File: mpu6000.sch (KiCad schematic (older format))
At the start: 9 parts

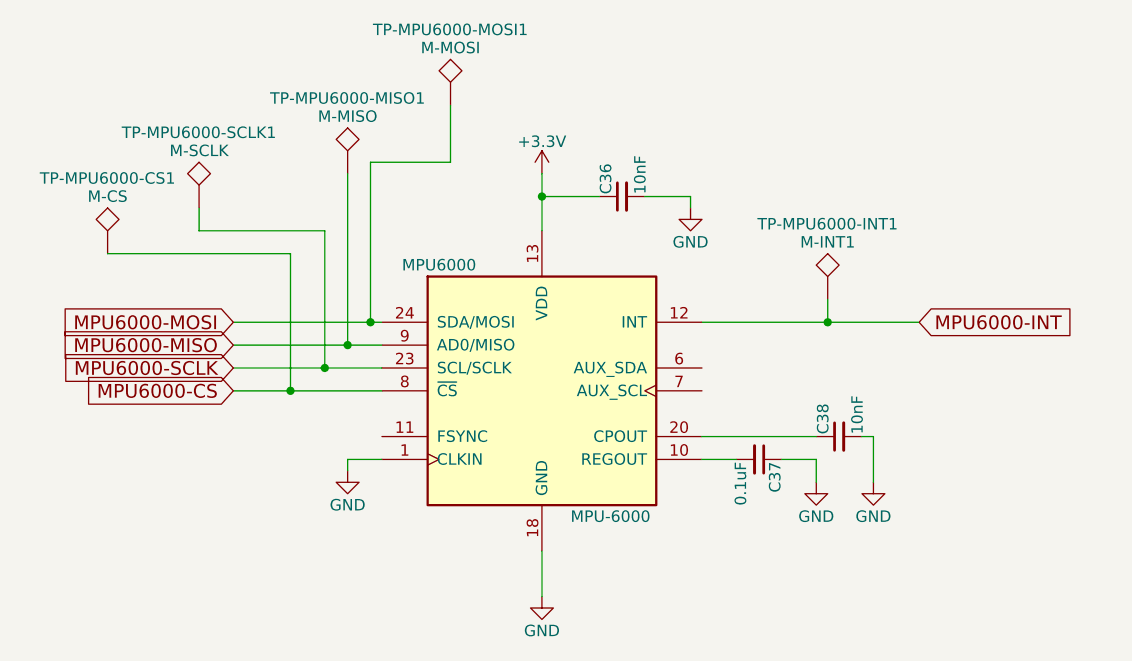
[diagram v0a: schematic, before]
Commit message: tp name fixes
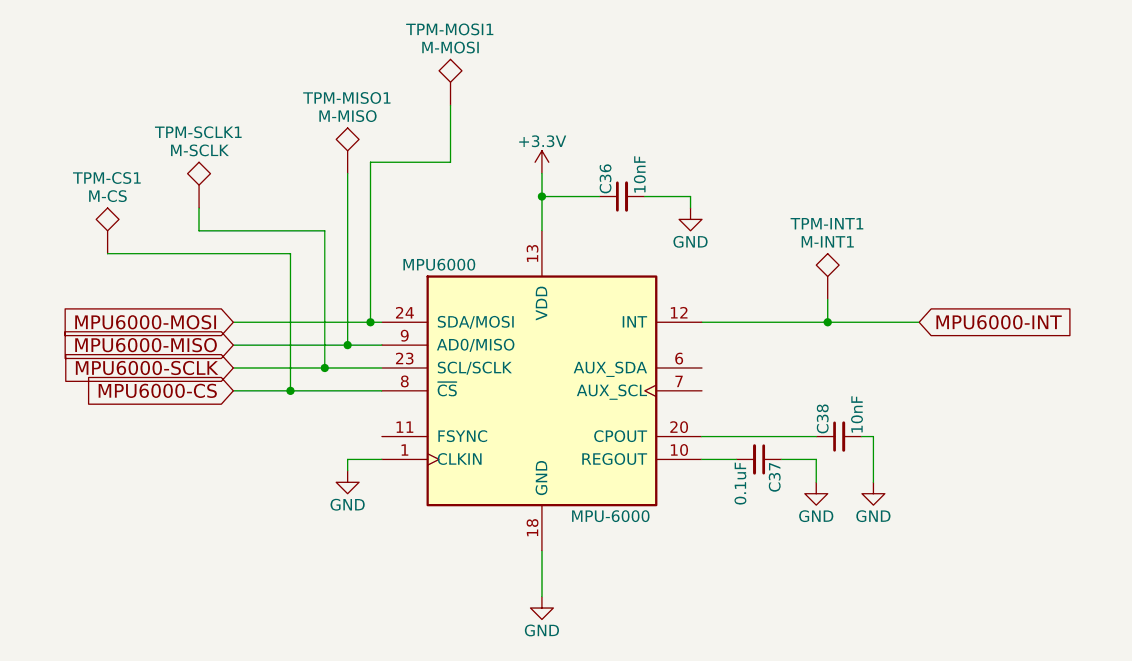
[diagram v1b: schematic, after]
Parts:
- renumbered TP-MPU6000-CS1 to TPM-CS1, TP-MPU6000-INT1 to TPM-INT1, TP-MPU6000-MISO1 to TPM-MISO1, TP-MPU6000-MOSI1 to TPM-MOSI1, TP-MPU6000-SCLK1 to TPM-SCLK1
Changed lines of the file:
@@
 	5100 4100 5100 4150
 $Comp
-L TEST TP-MPU6000-CS1
+L TEST TPM-CS1
 U 1 1 5B3F20EC
 P 4050 3200
-F 0 "TP-MPU6000-CS1" H 4050 3500 50  0000 C BNN
+F 0 "TPM-CS1" H 4050 3500 50  0000 C BNN
 F 1 "M-CS" H 4050 3450 50  0000 C CNN
 F 2 "Measurement_Points:Measurement_Point_Round-SMD-Pad_Small" H 4050 3200 50  0001 C CNN
@@
 $EndComp
 $Comp
-L TEST TP-MPU6000-SCLK1
+L TEST TPM-SCLK1
 U 1 1 5B3F20FE
 P 4450 3000
-F 0 "TP-MPU6000-SCLK1" H 4450 3300 50  0000 C BNN
+F 0 "TPM-SCLK1" H 4450 3300 50  0000 C BNN
 F 1 "M-SCLK" H 4450 3250 50  0000 C CNN
 F 2 "Measurement_Points:Measurement_Point_Round-SMD-Pad_Small" H 4450 3000 50  0001 C CNN
@@
 $EndComp
 $Comp
-L TEST TP-MPU6000-MISO1
+L TEST TPM-MISO1
 U 1 1 5B3F2136
 P 5100 2850
-F 0 "TP-MPU6000-MISO1" H 5100 3150 50  0000 C BNN
+F 0 "TPM-MISO1" H 5100 3150 50  0000 C BNN
 F 1 "M-MISO" H 5100 3100 50  0000 C CNN
 F 2 "Measurement_Points:Measurement_Point_Round-SMD-Pad_Small" H 5100 2850 50  0001 C CNN
@@
 $EndComp
 $Comp
-L TEST TP-MPU6000-MOSI1
+L TEST TPM-MOSI1
 U 1 1 5B3F216D
 P 5550 2550
-F 0 "TP-MPU6000-MOSI1" H 5550 2850 50  0000 C BNN
+F 0 "TPM-MOSI1" H 5550 2850 50  0000 C BNN
 F 1 "M-MOSI" H 5550 2800 50  0000 C CNN
 F 2 "Measurement_Points:Measurement_Point_Round-SMD-Pad_Small" H 5550 2550 50  0001 C CNN
@@
 $EndComp
 $Comp
-L TEST TP-MPU6000-INT1
+L TEST TPM-INT1
 U 1 1 5B3F2199
 P 7200 3400
-F 0 "TP-MPU6000-INT1" H 7200 3700 50  0000 C BNN
+F 0 "TPM-INT1" H 7200 3700 50  0000 C BNN
 F 1 "M-INT1" H 7200 3650 50  0000 C CNN
 F 2 "Measurement_Points:Measurement_Point_Round-SMD-Pad_Small" H 7200 3400 50  0001 C CNN

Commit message: Name changes on silk
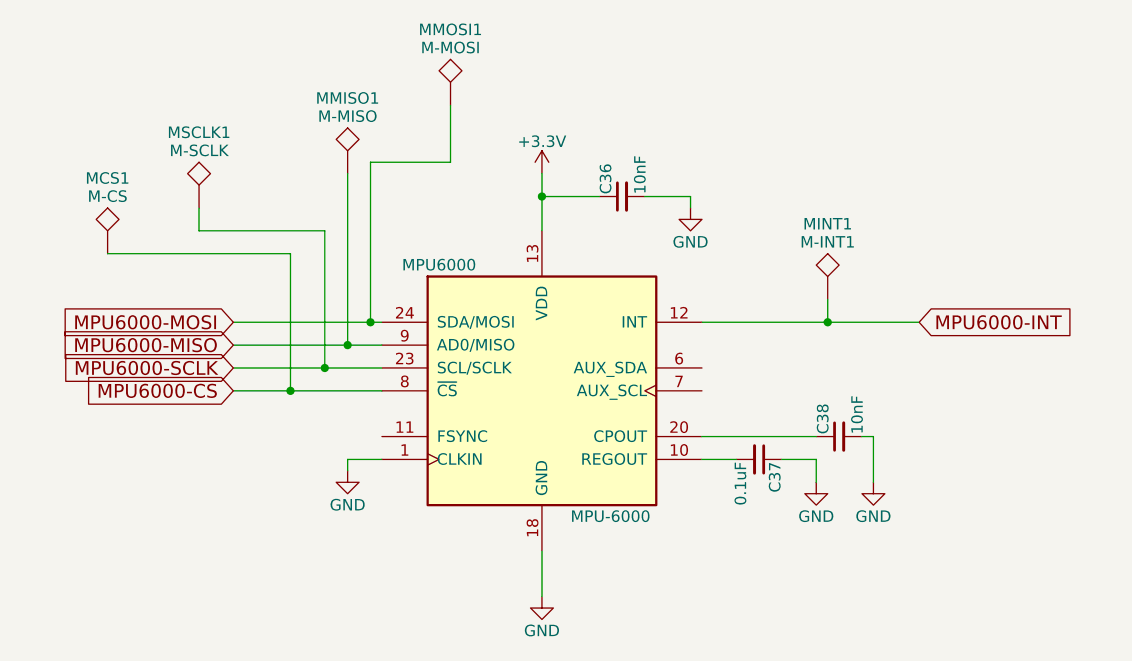
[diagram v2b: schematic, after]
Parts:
- renumbered TPM-CS1 to MCS1, TPM-INT1 to MINT1, TPM-MISO1 to MMISO1, TPM-MOSI1 to MMOSI1, TPM-SCLK1 to MSCLK1
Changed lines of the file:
@@
 	6650 3500 7600 3500
 $Comp
-L +3.3V #PWR38
+L +3.3V #PWR037
 U 1 1 5B360D5D
 P 5950 2850
-F 0 "#PWR38" H 5950 2700 50  0001 C CNN
+F 0 "#PWR037" H 5950 2700 50  0001 C CNN
 F 1 "+3.3V" H 5950 2990 50  0000 C CNN
 F 2 "" H 5950 2850 50  0001 C CNN
@@
 $EndComp
 $Comp
-L GND #PWR39
+L GND #PWR038
 U 1 1 5B360D77
 P 5950 4700
-F 0 "#PWR39" H 5950 4450 50  0001 C CNN
+F 0 "#PWR038" H 5950 4450 50  0001 C CNN
 F 1 "GND" H 5950 4550 50  0000 C CNN
 F 2 "" H 5950 4700 50  0001 C CNN
@@
 	5950 2850 5950 3100
 $Comp
-L GND #PWR42
+L GND #PWR039
 U 1 1 5B360DB0
 P 7400 4200
-F 0 "#PWR42" H 7400 3950 50  0001 C CNN
+F 0 "#PWR039" H 7400 3950 50  0001 C CNN
 F 1 "GND" H 7400 4050 50  0000 C CNN
 F 2 "" H 7400 4200 50  0001 C CNN
@@
 $EndComp
 $Comp
-L GND #PWR41
+L GND #PWR040
 U 1 1 5B360DCD
 P 7150 4200
-F 0 "#PWR41" H 7150 3950 50  0001 C CNN
+F 0 "#PWR040" H 7150 3950 50  0001 C CNN
 F 1 "GND" H 7150 4050 50  0000 C CNN
 F 2 "" H 7150 4200 50  0001 C CNN
@@
 $EndComp
 $Comp
-L GND #PWR40
+L GND #PWR041
 U 1 1 5B3610B5
 P 6600 3000
-F 0 "#PWR40" H 6600 2750 50  0001 C CNN
+F 0 "#PWR041" H 6600 2750 50  0001 C CNN
 F 1 "GND" H 6600 2850 50  0000 C CNN
 F 2 "" H 6600 3000 50  0001 C CNN
@@
 	6600 2950 6600 3000
 $Comp
-L GND #PWR37
+L GND #PWR042
 U 1 1 5B3610F5
 P 5100 4150
-F 0 "#PWR37" H 5100 3900 50  0001 C CNN
+F 0 "#PWR042" H 5100 3900 50  0001 C CNN
 F 1 "GND" H 5100 4000 50  0000 C CNN
 F 2 "" H 5100 4150 50  0001 C CNN
@@
 	5100 4100 5100 4150
 $Comp
-L TEST TPM-CS1
+L TEST MCS1
 U 1 1 5B3F20EC
 P 4050 3200
-F 0 "TPM-CS1" H 4050 3500 50  0000 C BNN
+F 0 "MCS1" H 4050 3500 50  0000 C BNN
 F 1 "M-CS" H 4050 3450 50  0000 C CNN
 F 2 "Measurement_Points:Measurement_Point_Round-SMD-Pad_Small" H 4050 3200 50  0001 C CNN
@@
 $EndComp
 $Comp
-L TEST TPM-SCLK1
+L TEST MSCLK1
 U 1 1 5B3F20FE
 P 4450 3000
-F 0 "TPM-SCLK1" H 4450 3300 50  0000 C BNN
+F 0 "MSCLK1" H 4450 3300 50  0000 C BNN
 F 1 "M-SCLK" H 4450 3250 50  0000 C CNN
 F 2 "Measurement_Points:Measurement_Point_Round-SMD-Pad_Small" H 4450 3000 50  0001 C CNN
@@
 $EndComp
 $Comp
-L TEST TPM-MISO1
+L TEST MMISO1
 U 1 1 5B3F2136
 P 5100 2850
-F 0 "TPM-MISO1" H 5100 3150 50  0000 C BNN
+F 0 "MMISO1" H 5100 3150 50  0000 C BNN
 F 1 "M-MISO" H 5100 3100 50  0000 C CNN
 F 2 "Measurement_Points:Measurement_Point_Round-SMD-Pad_Small" H 5100 2850 50  0001 C CNN
@@
 $EndComp
 $Comp
-L TEST TPM-MOSI1
+L TEST MMOSI1
 U 1 1 5B3F216D
 P 5550 2550
-F 0 "TPM-MOSI1" H 5550 2850 50  0000 C BNN
+F 0 "MMOSI1" H 5550 2850 50  0000 C BNN
 F 1 "M-MOSI" H 5550 2800 50  0000 C CNN
 F 2 "Measurement_Points:Measurement_Point_Round-SMD-Pad_Small" H 5550 2550 50  0001 C CNN
@@
 $EndComp
 $Comp
-L TEST TPM-INT1
+L TEST MINT1
 U 1 1 5B3F2199
 P 7200 3400
-F 0 "TPM-INT1" H 7200 3700 50  0000 C BNN
+F 0 "MINT1" H 7200 3700 50  0000 C BNN
 F 1 "M-INT1" H 7200 3650 50  0000 C CNN
 F 2 "Measurement_Points:Measurement_Point_Round-SMD-Pad_Small" H 7200 3400 50  0001 C CNN

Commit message: Changed MPU6000 footprint to one without the die pad
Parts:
- MPU6000: footprint Housings_DFN_QFN:QFN-24-1EP_4x4mm_Pitch0.5mm -> Housings_DFN_QFN:QFN-24_4x4mm_Pitch0.5mm
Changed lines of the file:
@@
 F 0 "MPU6000" H 5500 4350 50  0000 C CNN
 F 1 "MPU-6000" H 6250 3250 50  0000 C CNN
-F 2 "Housings_DFN_QFN:QFN-24-1EP_4x4mm_Pitch0.5mm" H 5950 3000 50  0001 C CNN
+F 2 "Housings_DFN_QFN:QFN-24_4x4mm_Pitch0.5mm" H 5950 3000 50  0001 C CNN
 F 3 "" H 5950 3650 50  0001 C CNN
 	1    5950 3800
